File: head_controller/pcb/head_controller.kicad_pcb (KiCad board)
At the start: 2 copper layers, 118.1 x 54.6 mm, 64 parts, among them P1 PWR_JACK_2.5x5.5, P2 HEADER_01X03, P3 BNC_DOUBLE_RA, P4 HEADER_02X08_SMD, P5 HEADER_02X08_SMD, P6 HEADER_02X08_SMD, P7 HEADER_02X08_SMD, SW1 SPST_SERIES_M, SW2 KT_SWITCH, U1 MAX6817, U2 MAX6817, U3 TLE723X, U4 TLE723X, U5 TLE723X, U6 TLE723X

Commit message: Initial board outline.
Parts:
- removed ARDUINO1: ARDUINO_MEGA, head_controller:ARDUINO_MEGA_SHIELD
- removed C1, C2, C3: 10uF, head_controller:SM1210
- removed C4, C5, C6, C7, C8, C9: 0.1uF, head_controller:SM1210
- removed D1, D10, D11, D12, D13, D14, D15, D16, D17, D18, D19, D2, D20, D21, D22, D23, D24, D25, D26, D27, D28, D29, D3, D30, D31, D32, D33, D4, D5, D6, D7, D8, D9: LED_24V, head_controller:LED_555-3XXX
- removed E1: ENCODER_C14, head_controller:Micro-MaTch_6_SMD
- removed P1: PWR_JACK_2.5x5.5, head_controller:DCJACK_2PIN_HIGHCURRENT
- removed P2: HEADER_01X03, footprints:Header_3_Pin
- removed P3: BNC_DOUBLE_RA, head_controller:BNC_DOUBLE
- removed P4, P5, P6, P7: HEADER_02X08_SMD, head_controller:HEADER_02x08_SMD
- removed R1, R2, R3: 5.11k, head_controller:SM1210
- removed REG1: CONV_DC_DC_12V_1A, head_controller:DC_DC_CONV_R78C
- removed S1: HEADER_01X02_SHR, head_controller:Header_Shrouded_2_Pin
- removed SW1: SPST_SERIES_M, head_controller:SPST_SERIES_M
- removed SW2: KT_SWITCH, head_controller:KT_SWITCH
- removed U1, U2: MAX6817, head_controller:MAX6817
- removed U3, U4, U5, U6: TLE723X, head_controller:TLE723X
- added REF**: mounting_hole, head_controller:mounting_hole, F.Cu at (43.2, 55.9)
- added REF**: mounting_hole, head_controller:mounting_hole, F.Cu at (81.3, 27.9)
- added REF**: mounting_hole, head_controller:mounting_hole, F.Cu at (27.9, 66.0)
- added REF**: mounting_hole, head_controller:mounting_hole, F.Cu at (81.3, 66.0)
- added REF**: mounting_hole, head_controller:mounting_hole, F.Cu at (27.9, 119.4)
- added REF**: mounting_hole, head_controller:mounting_hole, F.Cu at (81.3, 119.4)
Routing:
- net GND: track 445.6 -> 0.00 mm, vias 6 -> 0
- net +5V: track 260.3 -> 0.00 mm, vias 1 -> 0
- net VAA: track 203.1 -> 0.00 mm, vias 1 -> 0
- net /LED_PWR: track 184.2 -> 0.00 mm, vias 3 -> 0
- net /CS: track 171.1 -> 0.00 mm, vias 3 -> 0
- net /RST: track 164.0 -> 0.00 mm, vias 3 -> 0
- net /SCK: track 153.6 -> 0.00 mm, vias 4 -> 0
- net /IN: track 141.0 -> 0.00 mm, vias 5 -> 0
- net /ENC_B: track 104.7 -> 0.00 mm, vias 1 -> 0
- net /TX3: track 98.4 -> 0.00 mm
- net /MISO: track 77.6 -> 0.00 mm, vias 2 -> 0
- net /BNC_A: track 76.7 -> 0.00 mm
- net /V_IN: track 69.0 -> 0.00 mm, vias 1 -> 0
- net /MOSI: track 65.0 -> 0.00 mm, vias 1 -> 0
- net /BNC_B: track 62.5 -> 0.00 mm
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- removed copper zone on B.Cu, net GND
- removed copper zone on F.Cu, net VAA
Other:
- board size 118.1 x 54.6 mm -> 59.3 x 132.3 mm
- net class Default: clearance 0.254 -> 0.2; trace_width 0.254 -> 0.25; via_dia 0.889 -> 0.6; via_drill 0.635 -> 0.4
- net class GND removed
- net class LEDPOWER removed
- net class POWER removed
- net class SIGNAL removed
- net class SUPERPOWER removed
- rule pad_to_mask_clearance: 0 -> 0.2
- rule trace_clearance: 0.254 -> 0.2
- rule trace_min: 0.254 -> 0.2
- rule via_min_drill: 0.508 -> 0.3
- rule via_min_size: 0.889 -> 0.4
- board text removed: "+"
- board text removed: "+24VDC"
- board text removed: "-"
- board text removed: "0"
- board text removed: "1"
- board text removed: "10"
- board text removed: "11"
- board text removed: "12"
- board text removed: "12V_DC_DC"
- board text removed: "13"
- board text removed: "14"
- board text removed: "15"
- board text removed: "16"
- board text removed: "17"
- board text removed: "18"
- board text removed: "19"
- board text removed: "2"
- board text removed: "20"
- board text removed: "21"
- board text removed: "22"
- board text removed: "23"
- board text removed: "24"
- board text removed: "25"
- board text removed: "26"
- board text removed: "27"
- board text removed: "28"
- board text removed: "29"
- board text removed: "3"
- board text removed: "30"
- board text removed: "31"
- board text removed: "4"
- board text removed: "5"
- board text removed: "6"
- board text removed: "7"
- board text removed: "8"
- board text removed: "9"
- board text removed: "DISPLAY"
- board text removed: "Janelia Modular Device head_controller model_number: 1110 02/2015 version 1.2"
- board text removed: "SWITCH"
- board text removed: "https://github.com/JaneliaSciComp/modular-devices"

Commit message: Test gerbers.
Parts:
- added REF**: valve_hole, head_controller:valve_hole, F.Cu at (76.2, 76.2)
- added REF**: valve_hole, head_controller:valve_hole, F.Cu at (35.6, 116.8)
- added REF**: valve_hole, head_controller:valve_hole, F.Cu at (73.7, 116.8)
- added REF**: valve_hole, head_controller:valve_hole, F.Cu at (53.3, 149.9)
- added REF**: valve_hole, head_controller:valve_hole, F.Cu at (42.9, 42.7)
- added REF**: valve_hole, head_controller:valve_hole, F.Cu at (78.5, 36.1)
- added REF**: valve_hole, head_controller:valve_hole, F.Cu at (33.0, 73.7)
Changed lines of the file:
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@@
     (links 0)
     (no_connects 0)
-    (area 0 0 0 0)
+    (area 22.173772 24.3364 87.046228 157.772101)
     (thickness 1.6)
     (drawings 14)
     (tracks 0)
     (zones 0)
-    (modules 6)
+    (modules 13)
     (nets 1)
   )
@@
     (mod_text_size 1 1)
     (mod_text_width 0.15)
-    (pad_size 3.81 3.81)
-    (pad_drill 2.8448)
+    (pad_size 7.874 7.874)
+    (pad_drill 7.366)
     (pad_to_mask_clearance 0.2)
     (aux_axis_origin 0 0)
     (visible_elements FFFFFF7F)
     (pcbplotparams
-      (layerselection 0x00030_80000001)
-      (usegerberextensions false)
-      (excludeedgelayer true)
+      (layerselection 0x000f0_80000001)
+      (usegerberextensions true)
+      (excludeedgelayer false)
       (linewidth 0.100000)
       (plotframeref false)
@@
       (plotinvisibletext false)
       (padsonsilk false)
-      (subtractmaskfromsilk false)
+      (subtractmaskfromsilk true)
       (outputformat 1)
       (mirror false)
-      (drillshape 1)
+      (drillshape 0)
       (scaleselection 1)
-      (outputdirectory ""))
+      (outputdirectory gerbers/))
   )
   (net 0 "")
@@
     (pad "" thru_hole circle (at 0.5842 0.5334) (size 3.81 3.81) (drill 2.8448) (layers *.Cu *.Mask F.SilkS))
   )
+  (module head_controller:valve_hole (layer F.Cu)
+    (at 42.926 42.672)
+    (fp_text reference REF** (at 0 5.08) (layer F.SilkS) hide
+      (effects (font (size 1.016 1.016) (thickness 0.1016)))
+    )
+    (fp_text value valve_hole (at 0 -5.08) (layer F.SilkS) hide
+      (effects (font (size 1.016 1.016) (thickness 0.1016)))
+    )
+    (pad "" thru_hole circle (at -11.8364 -6.1722) (size 7.874 7.874) (drill 7.366) (layers *.Cu *.Mask F.SilkS))
+  )
+  (module head_controller:valve_hole (layer F.Cu)
+    (at 78.486 36.068)
+    (fp_text reference REF** (at 0 5.08) (layer F.SilkS) hide
+      (effects (font (size 1.016 1.016) (thickness 0.1016)))
+    )
+    (fp_text value valve_hole (at 0 -5.08) (layer F.SilkS) hide
+      (effects (font (size 1.016 1.016) (thickness 0.1016)))
+    )
+    (pad "" thru_hole circle (at 0.4572 0.4318) (size 7.874 7.874) (drill 7.366) (layers *.Cu *.Mask F.SilkS))
+  )
+  (module head_controller:valve_hole (layer F.Cu)
+    (at 33.02 73.66)
+    (fp_text reference REF** (at 0 5.08) (layer F.SilkS) hide
+      (effects (font (size 1.016 1.016) (thickness 0.1016)))
+    )
+    (fp_text value valve_hole (at 0 -5.08) (layer F.SilkS) hide
+      (effects (font (size 1.016 1.016) (thickness 0.1016)))
+    )
+    (pad "" thru_hole circle (at -1.9304 0.381) (size 7.874 7.874) (drill 7.366) (layers *.Cu *.Mask F.SilkS))
+  )
+  (module head_controller:valve_hole (layer F.Cu)
+    (at 76.2 76.2)
+    (fp_text reference REF** (at 0 5.08) (layer F.SilkS) hide
+      (effects (font (size 1.016 1.016) (thickness 0.1016)))
+    )
+    (fp_text value valve_hole (at 0 -5.08) (layer F.SilkS) hide
+      (effects (font (size 1.016 1.016) (thickness 0.1016)))
+    )
+    (pad "" thru_hole circle (at 2.7432 -2.159) (size 7.874 7.874) (drill 7.366) (layers *.Cu *.Mask F.SilkS))
+  )
+  (module head_controller:valve_hole (layer F.Cu)
+    (at 35.56 116.84)
+    (fp_text reference REF** (at 0 5.08) (layer F.SilkS) hide
+      (effects (font (size 1.016 1.016) (thickness 0.1016)))
+    )
+    (fp_text value valve_hole (at 0 -5.08) (layer F.SilkS) hide
+      (effects (font (size 1.016 1.016) (thickness 0.1016)))
+    )
+    (pad "" thru_hole circle (at -4.4704 -5.2324) (size 7.874 7.874) (drill 7.366) (layers *.Cu *.Mask F.SilkS))
+  )
+  (module head_controller:valve_hole (layer F.Cu)
+    (at 73.66 116.84)
+    (fp_text reference REF** (at 0 5.08) (layer F.SilkS) hide
+      (effects (font (size 1.016 1.016) (thickness 0.1016)))
+    )
+    (fp_text value valve_hole (at 0 -5.08) (layer F.SilkS) hide
+      (effects (font (size 1.016 1.016) (thickness 0.1016)))
+    )
+    (pad "" thru_hole circle (at 5.2832 -5.2324) (size 7.874 7.874) (drill 7.366) (layers *.Cu *.Mask F.SilkS))
+  )
+  (module head_controller:valve_hole (layer F.Cu)
+    (at 53.34 149.86)
+    (fp_text reference REF** (at 0 5.08) (layer F.SilkS) hide
+      (effects (font (size 1.016 1.016) (thickness 0.1016)))
+    )
+    (fp_text value valve_hole (at 0 -5.08) (layer F.SilkS) hide
+      (effects (font (size 1.016 1.016) (thickness 0.1016)))
+    )
+    (pad "" thru_hole circle (at 1.6764 2.1082) (size 7.874 7.874) (drill 7.366) (layers *.Cu *.Mask F.SilkS))
+  )
   (gr_arc (start 55.0164 151.9682) (end 60.706 151.9682) (angle 180) (layer Edge.Cuts) (width 0.2286))

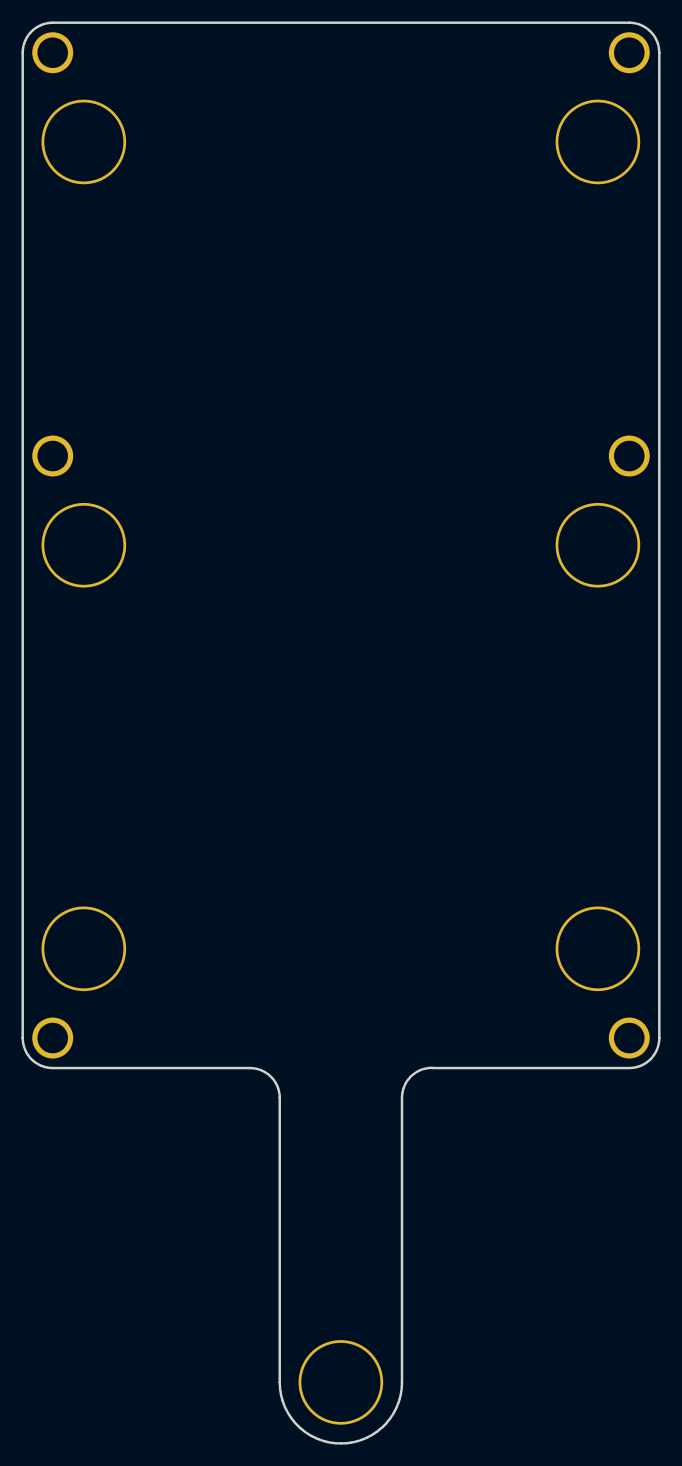
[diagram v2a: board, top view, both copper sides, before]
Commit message: Added valve controls to schematic.
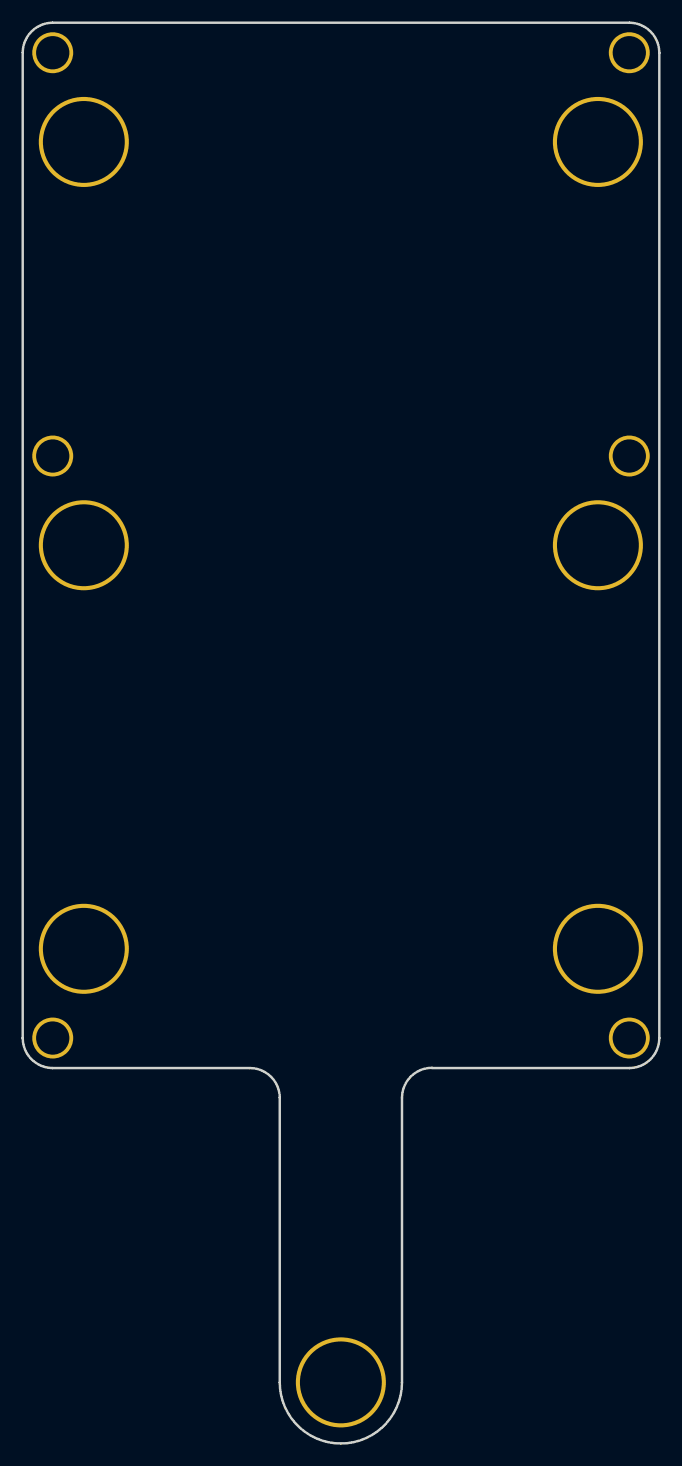
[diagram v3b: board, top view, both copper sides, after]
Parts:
- moved REF** 31.5 mm to (28.2, 28.2)
- moved REF** 13.3 mm to (31.1, 36.5)
- moved REF** 7.44 mm to (78.9, 111.6)
- moved REF** 6.88 mm to (31.1, 111.6)
- moved REF** 3.49 mm to (78.9, 74.0)
- moved REF** 2.69 mm to (55.0, 152.0)
- moved REF** 1.97 mm to (31.1, 74.0)
- moved REF** 0.79 mm to (81.9, 119.9)
- moved REF** 0.66 mm to (81.9, 65.7)
- moved REF** 0.64 mm to (81.9, 28.2)
- moved REF** 0.63 mm to (78.9, 36.5)
- moved REF** 0.59 mm to (28.2, 119.9)
- moved REF** 0.40 mm to (28.2, 65.7)
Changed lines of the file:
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@@
     (mod_text_size 1 1)
     (mod_text_width 0.15)
-    (pad_size 7.874 7.874)
-    (pad_drill 7.366)
+    (pad_size 8.382 8.382)
+    (pad_drill 7.62)
     (pad_to_mask_clearance 0.2)
     (aux_axis_origin 0 0)
@@
   )
   (module head_controller:mounting_hole (layer F.Cu)
-    (at 43.18 55.88)
+    (at 81.8642 119.9134)
     (fp_text reference REF** (at 0 2.54) (layer F.SilkS) hide
       (effects (font (size 1.016 1.016) (thickness 0.1016)))
@@
       (effects (font (size 1.016 1.016) (thickness 0.1016)))
     )
-    (pad "" thru_hole circle (at -14.986 -27.686) (size 3.81 3.81) (drill 2.8448) (layers *.Cu *.Mask F.SilkS))
+    (pad "" thru_hole circle (at 0 0) (size 3.81 3.81) (drill 3.0988) (layers *.Cu *.Mask F.SilkS))
   )
   (module head_controller:mounting_hole (layer F.Cu)
-    (at 81.28 27.94)
+    (at 28.194 119.9134)
     (fp_text reference REF** (at 0 2.54) (layer F.SilkS) hide
       (effects (font (size 1.016 1.016) (thickness 0.1016)))
@@
       (effects (font (size 1.016 1.016) (thickness 0.1016)))
     )
-    (pad "" thru_hole circle (at 0.5842 0.254) (size 3.81 3.81) (drill 2.8448) (layers *.Cu *.Mask F.SilkS))
+    (pad "" thru_hole circle (at 0 0) (size 3.81 3.81) (drill 3.0988) (layers *.Cu *.Mask F.SilkS))
   )
   (module head_controller:mounting_hole (layer F.Cu)
-    (at 27.94 66.04)
+    (at 81.8642 65.7352)
     (fp_text reference REF** (at 0 2.54) (layer F.SilkS) hide
       (effects (font (size 1.016 1.016) (thickness 0.1016)))
@@
       (effects (font (size 1.016 1.016) (thickness 0.1016)))
     )
-    (pad "" thru_hole circle (at 0.254 -0.3048) (size 3.81 3.81) (drill 2.8448) (layers *.Cu *.Mask F.SilkS))
+    (pad "" thru_hole circle (at 0 0) (size 3.81 3.81) (drill 3.0988) (layers *.Cu *.Mask F.SilkS))
   )
   (module head_controller:mounting_hole (layer F.Cu)
-    (at 81.28 66.04)
+    (at 28.194 65.7352)
     (fp_text reference REF** (at 0 2.54) (layer F.SilkS) hide
       (effects (font (size 1.016 1.016) (thickness 0.1016)))
@@
       (effects (font (size 1.016 1.016) (thickness 0.1016)))
     )
-    (pad "" thru_hole circle (at 0.5842 -0.3048) (size 3.81 3.81) (drill 2.8448) (layers *.Cu *.Mask F.SilkS))
+    (pad "" thru_hole circle (at 0 0) (size 3.81 3.81) (drill 3.0988) (layers *.Cu *.Mask F.SilkS))
   )
   (module head_controller:mounting_hole (layer F.Cu)
-    (at 27.94 119.38)
+    (at 81.8642 28.194)
     (fp_text reference REF** (at 0 2.54) (layer F.SilkS) hide
       (effects (font (size 1.016 1.016) (thickness 0.1016)))
@@
       (effects (font (size 1.016 1.016) (thickness 0.1016)))
     )
-    (pad "" thru_hole circle (at 0.254 0.5334) (size 3.81 3.81) (drill 2.8448) (layers *.Cu *.Mask F.SilkS))
+    (pad "" thru_hole circle (at 0 0) (size 3.81 3.81) (drill 3.0988) (layers *.Cu *.Mask F.SilkS))
   )
   (module head_controller:mounting_hole (layer F.Cu)
-    (at 81.28 119.38)
+    (at 28.194 28.194)
     (fp_text reference REF** (at 0 2.54) (layer F.SilkS) hide
       (effects (font (size 1.016 1.016) (thickness 0.1016)))
@@
       (effects (font (size 1.016 1.016) (thickness 0.1016)))
     )
-    (pad "" thru_hole circle (at 0.5842 0.5334) (size 3.81 3.81) (drill 2.8448) (layers *.Cu *.Mask F.SilkS))
+    (pad "" thru_hole circle (at 0 0) (size 3.81 3.81) (drill 3.0988) (layers *.Cu *.Mask F.SilkS))
   )
   (module head_controller:valve_hole (layer F.Cu)
-    (at 42.926 42.672)
+    (at 55.0164 151.9682)
     (fp_text reference REF** (at 0 5.08) (layer F.SilkS) hide
       (effects (font (size 1.016 1.016) (thickness 0.1016)))
@@
       (effects (font (size 1.016 1.016) (thickness 0.1016)))
     )
-    (pad "" thru_hole circle (at -11.8364 -6.1722) (size 7.874 7.874) (drill 7.366) (layers *.Cu *.Mask F.SilkS))
+    (pad "" thru_hole circle (at 0 0) (size 8.382 8.382) (drill 7.62) (layers *.Cu *.Mask F.SilkS))
   )
   (module head_controller:valve_hole (layer F.Cu)
-    (at 78.486 36.068)
+    (at 78.9432 111.6076)
     (fp_text reference REF** (at 0 5.08) (layer F.SilkS) hide
       (effects (font (size 1.016 1.016) (thickness 0.1016)))
@@
       (effects (font (size 1.016 1.016) (thickness 0.1016)))
     )
-    (pad "" thru_hole circle (at 0.4572 0.4318) (size 7.874 7.874) (drill 7.366) (layers *.Cu *.Mask F.SilkS))
+    (pad "" thru_hole circle (at 0 0) (size 8.382 8.382) (drill 7.62) (layers *.Cu *.Mask F.SilkS))
   )
   (module head_controller:valve_hole (layer F.Cu)
-    (at 33.02 73.66)
+    (at 31.0896 111.6076)
     (fp_text reference REF** (at 0 5.08) (layer F.SilkS) hide
       (effects (font (size 1.016 1.016) (thickness 0.1016)))
@@
       (effects (font (size 1.016 1.016) (thickness 0.1016)))
     )
-    (pad "" thru_hole circle (at -1.9304 0.381) (size 7.874 7.874) (drill 7.366) (layers *.Cu *.Mask F.SilkS))
+    (pad "" thru_hole circle (at 0 0) (size 8.382 8.382) (drill 7.62) (layers *.Cu *.Mask F.SilkS))
   )
   (module head_controller:valve_hole (layer F.Cu)
-    (at 76.2 76.2)
+    (at 78.9432 74.041)
     (fp_text reference REF** (at 0 5.08) (layer F.SilkS) hide
       (effects (font (size 1.016 1.016) (thickness 0.1016)))
@@
       (effects (font (size 1.016 1.016) (thickness 0.1016)))
     )
-    (pad "" thru_hole circle (at 2.7432 -2.159) (size 7.874 7.874) (drill 7.366) (layers *.Cu *.Mask F.SilkS))
+    (pad "" thru_hole circle (at 0 0) (size 8.382 8.382) (drill 7.62) (layers *.Cu *.Mask F.SilkS))
   )
   (module head_controller:valve_hole (layer F.Cu)
-    (at 35.56 116.84)
+    (at 31.0896 74.041)
     (fp_text reference REF** (at 0 5.08) (layer F.SilkS) hide
       (effects (font (size 1.016 1.016) (thickness 0.1016)))
@@
       (effects (font (size 1.016 1.016) (thickness 0.1016)))
     )
-    (pad "" thru_hole circle (at -4.4704 -5.2324) (size 7.874 7.874) (drill 7.366) (layers *.Cu *.Mask F.SilkS))
+    (pad "" thru_hole circle (at 0 0) (size 8.382 8.382) (drill 7.62) (layers *.Cu *.Mask F.SilkS))
   )
   (module head_controller:valve_hole (layer F.Cu)
-    (at 73.66 116.84)
+    (at 78.9432 36.4998)
     (fp_text reference REF** (at 0 5.08) (layer F.SilkS) hide
       (effects (font (size 1.016 1.016) (thickness 0.1016)))
@@
       (effects (font (size 1.016 1.016) (thickness 0.1016)))
     )
-    (pad "" thru_hole circle (at 5.2832 -5.2324) (size 7.874 7.874) (drill 7.366) (layers *.Cu *.Mask F.SilkS))
+    (pad "" thru_hole circle (at 0 0) (size 8.382 8.382) (drill 7.62) (layers *.Cu *.Mask F.SilkS))
   )
   (module head_controller:valve_hole (layer F.Cu)
-    (at 53.34 149.86)
+    (at 31.0896 36.4998)
     (fp_text reference REF** (at 0 5.08) (layer F.SilkS) hide
       (effects (font (size 1.016 1.016) (thickness 0.1016)))
@@
       (effects (font (size 1.016 1.016) (thickness 0.1016)))
     )
-    (pad "" thru_hole circle (at 1.6764 2.1082) (size 7.874 7.874) (drill 7.366) (layers *.Cu *.Mask F.SilkS))
+    (pad "" thru_hole circle (at 0 0) (size 8.382 8.382) (drill 7.62) (layers *.Cu *.Mask F.SilkS))
   )
   (gr_arc (start 55.0164 151.9682) (end 60.706 151.9682) (angle 180) (layer Edge.Cuts) (width 0.2286))

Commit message: Fixed typos.
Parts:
- added D1: LED_24V_SMD, head_controller:LED_555-3XXX_SMD, F.Cu at (44.5, 180.3)
- added D2: LED_24V_SMD, head_controller:LED_555-3XXX_SMD, F.Cu at (64.8, 177.8)
- added D3: LED_24V_SMD, head_controller:LED_555-3XXX_SMD, F.Cu at (41.9, 162.6)
- added D4: LED_24V_SMD, head_controller:LED_555-3XXX_SMD, F.Cu at (49.5, 184.2)
- added D5: LED_24V_SMD, head_controller:LED_555-3XXX_SMD, F.Cu at (59.7, 179.1)
- added D6: LED_24V_SMD, head_controller:LED_555-3XXX_SMD, F.Cu at (48.3, 163.8)
- added D7: LED_24V_SMD, head_controller:LED_555-3XXX_SMD, F.Cu at (62.2, 163.8)
- added P1: HEADER_02X08_SMD, head_controller:HEADER_02x08_SMD, F.Cu at (78.7, 92.7)
- added S1: HEADER_01X02_SMD, head_controller:Header_2_Pin_SMD, F.Cu at (81.3, 149.9)
- added S2: HEADER_01X02_SMD, head_controller:Header_2_Pin_SMD, F.Cu at (88.9, 161.3)
- added S3: HEADER_01X02_SMD, head_controller:Header_2_Pin_SMD, F.Cu at (114.3, 152.4)
- added S4: HEADER_01X02_SMD, head_controller:Header_2_Pin_SMD, F.Cu at (78.7, 174.0)
- added S5: HEADER_01X02_SMD, head_controller:Header_2_Pin_SMD, F.Cu at (71.1, 157.5)
- added S6: HEADER_01X02_SMD, head_controller:Header_2_Pin_SMD, F.Cu at (34.3, 166.4)
- added S7: HEADER_01X02_SMD, head_controller:Header_2_Pin_SMD, F.Cu at (33.0, 181.6)
